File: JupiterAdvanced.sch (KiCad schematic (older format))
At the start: 224 parts, among them SW1 SW_Push, U1 PRTR5V0U2X, U10 ATmega32U4-AU, Y1 16MHz

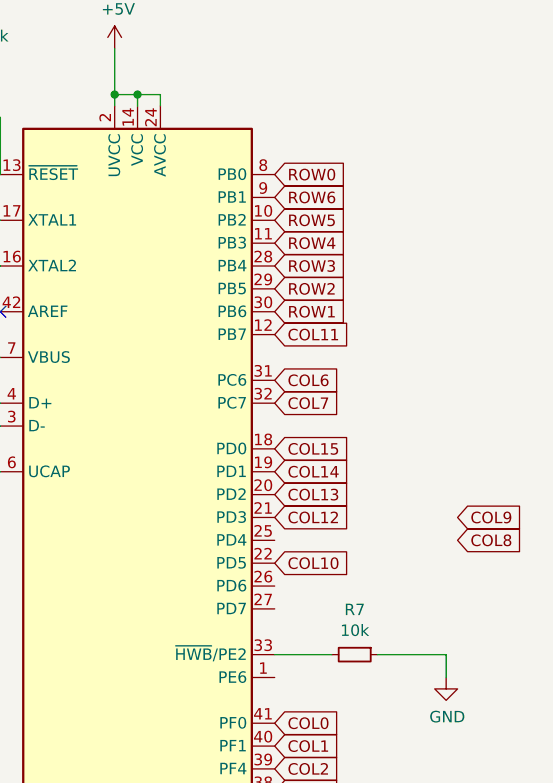
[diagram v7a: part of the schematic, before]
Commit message: Matrix reconnect, still missing some pins.
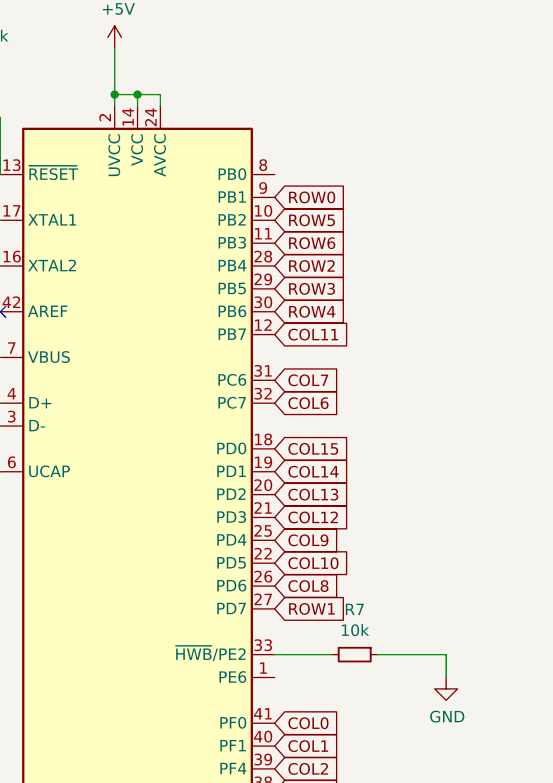
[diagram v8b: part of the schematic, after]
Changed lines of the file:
@@
 Text GLabel 12300 3550 2    50   Input ~ 0
 COL15
+Text GLabel 12300 2650 2    50   Input ~ 0
+ROW6
 Text GLabel 12300 2450 2    50   Input ~ 0
-ROW6
-Text GLabel 12300 2350 2    50   Input ~ 0
 ROW0
+Text GLabel 12300 3250 2    50   Input ~ 0
+COL7
 Text GLabel 12300 3350 2    50   Input ~ 0
-COL7
-Text GLabel 12300 3250 2    50   Input ~ 0
 COL6
 Text GLabel 12300 5250 2    50   Input ~ 0
@@
 Text GLabel 12300 3850 2    50   Input ~ 0
 COL12
-Text GLabel 13100 3850 2    50   Input ~ 0
+Text GLabel 12300 3950 2    50   Input ~ 0
 COL9
-Text GLabel 13100 3950 2    50   Input ~ 0
+Text GLabel 12300 4150 2    50   Input ~ 0
 COL8
 $Comp
@@
 Wire Wire Line
 	9600 2800 9750 2800
+Text GLabel 12300 4250 2    50   Input ~ 0
+ROW1
+Text GLabel 12300 2750 2    50   Input ~ 0
+ROW2
+Text GLabel 12300 2850 2    50   Input ~ 0
+ROW3
 Text GLabel 12300 2950 2    50   Input ~ 0
-ROW1
-Text GLabel 12300 2850 2    50   Input ~ 0
-ROW2
-Text GLabel 12300 2750 2    50   Input ~ 0
-ROW3
-Text GLabel 12300 2650 2    50   Input ~ 0
 ROW4
 Wire Wire Line
